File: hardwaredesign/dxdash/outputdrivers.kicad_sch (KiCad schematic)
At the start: 6 parts, among them J7 Power Low Side Outputs, Q2 NCV8402xST, Q3 NCV8402xST, U7 74HCT04

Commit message: controller board added features
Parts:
- renumbered J7 to J8
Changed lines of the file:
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@@
 		(dnp no)
 		(fields_autoplaced yes)
-		(property "Reference" "J7"
+		(property "Reference" "J8"
 			(at 149.86 100.3299 0)
 			(effects

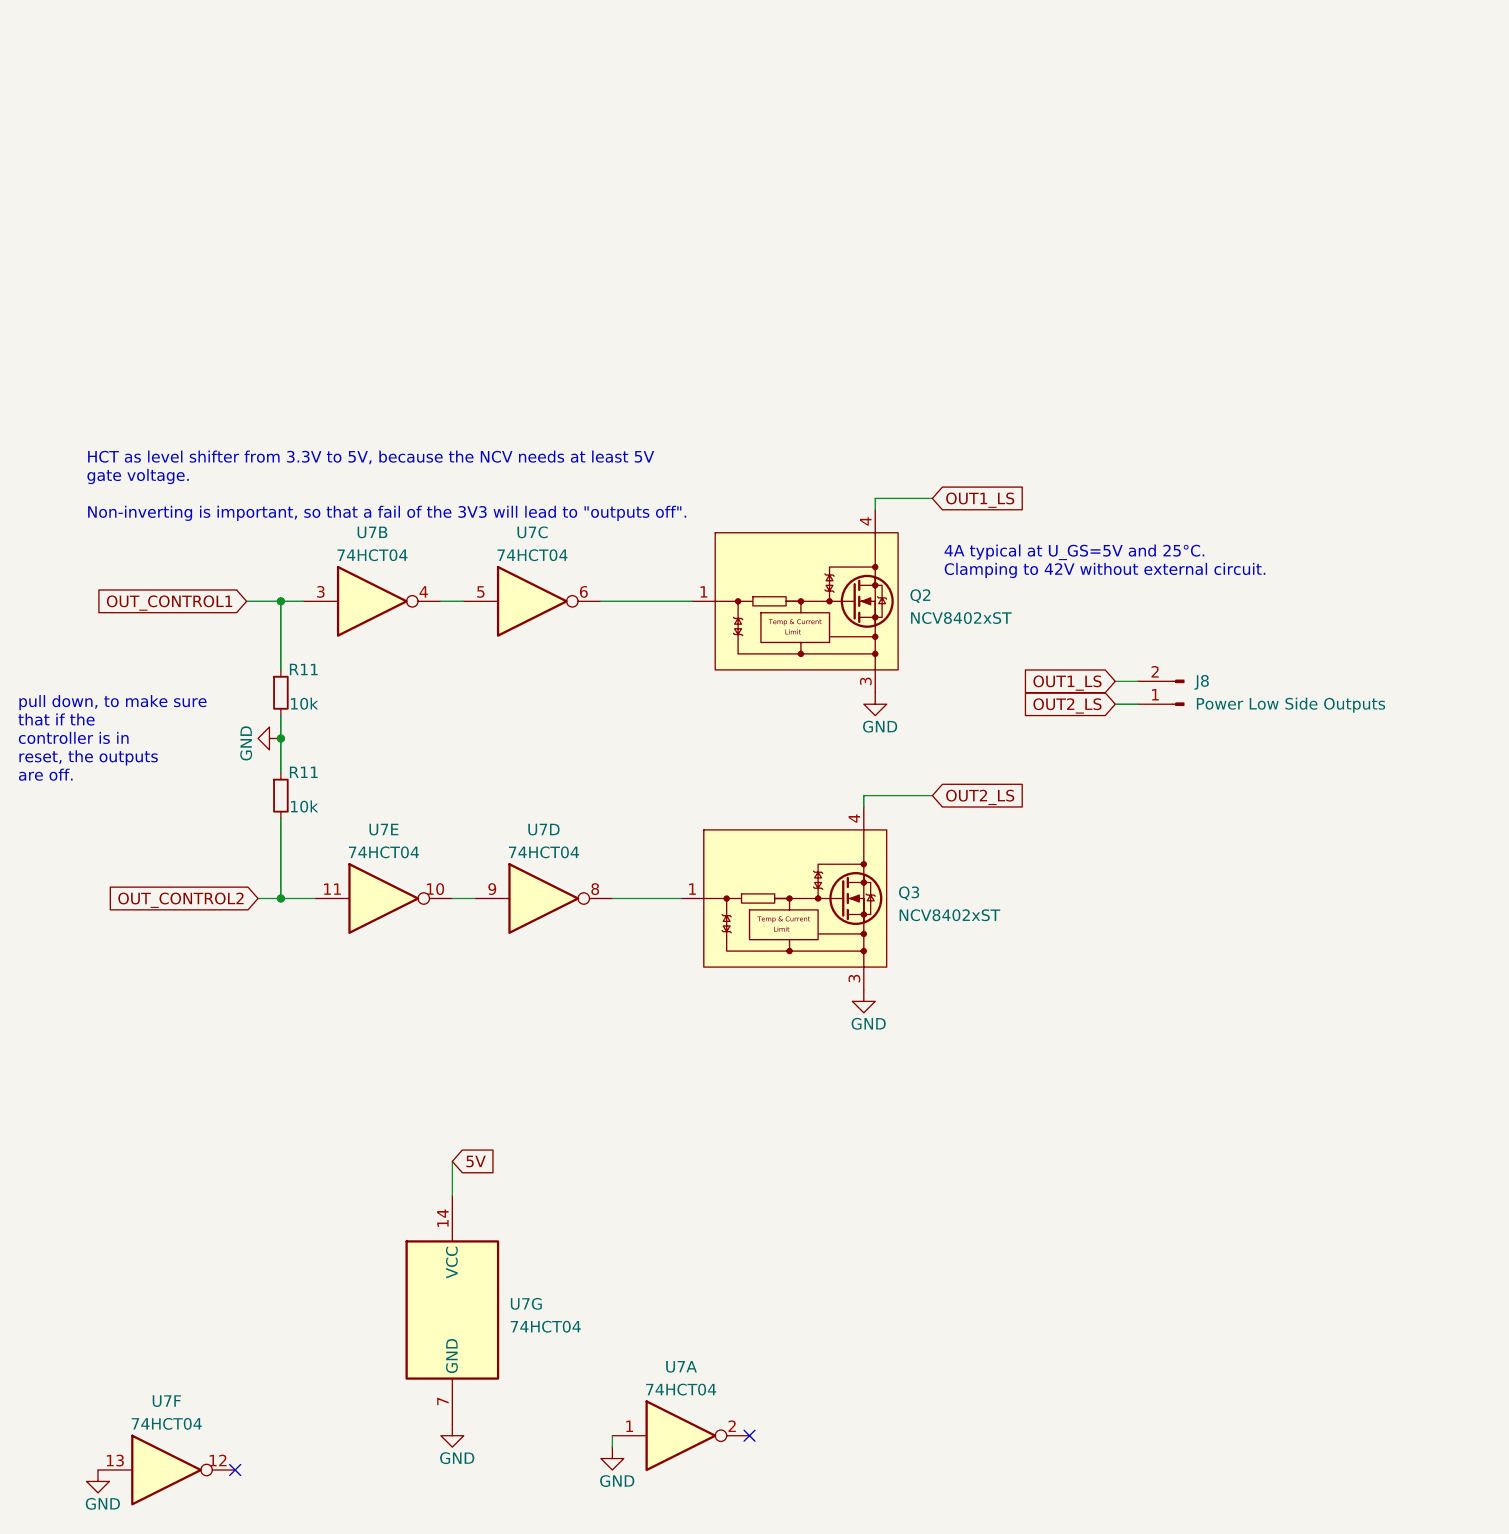
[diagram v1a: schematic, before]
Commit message: added polyfuses
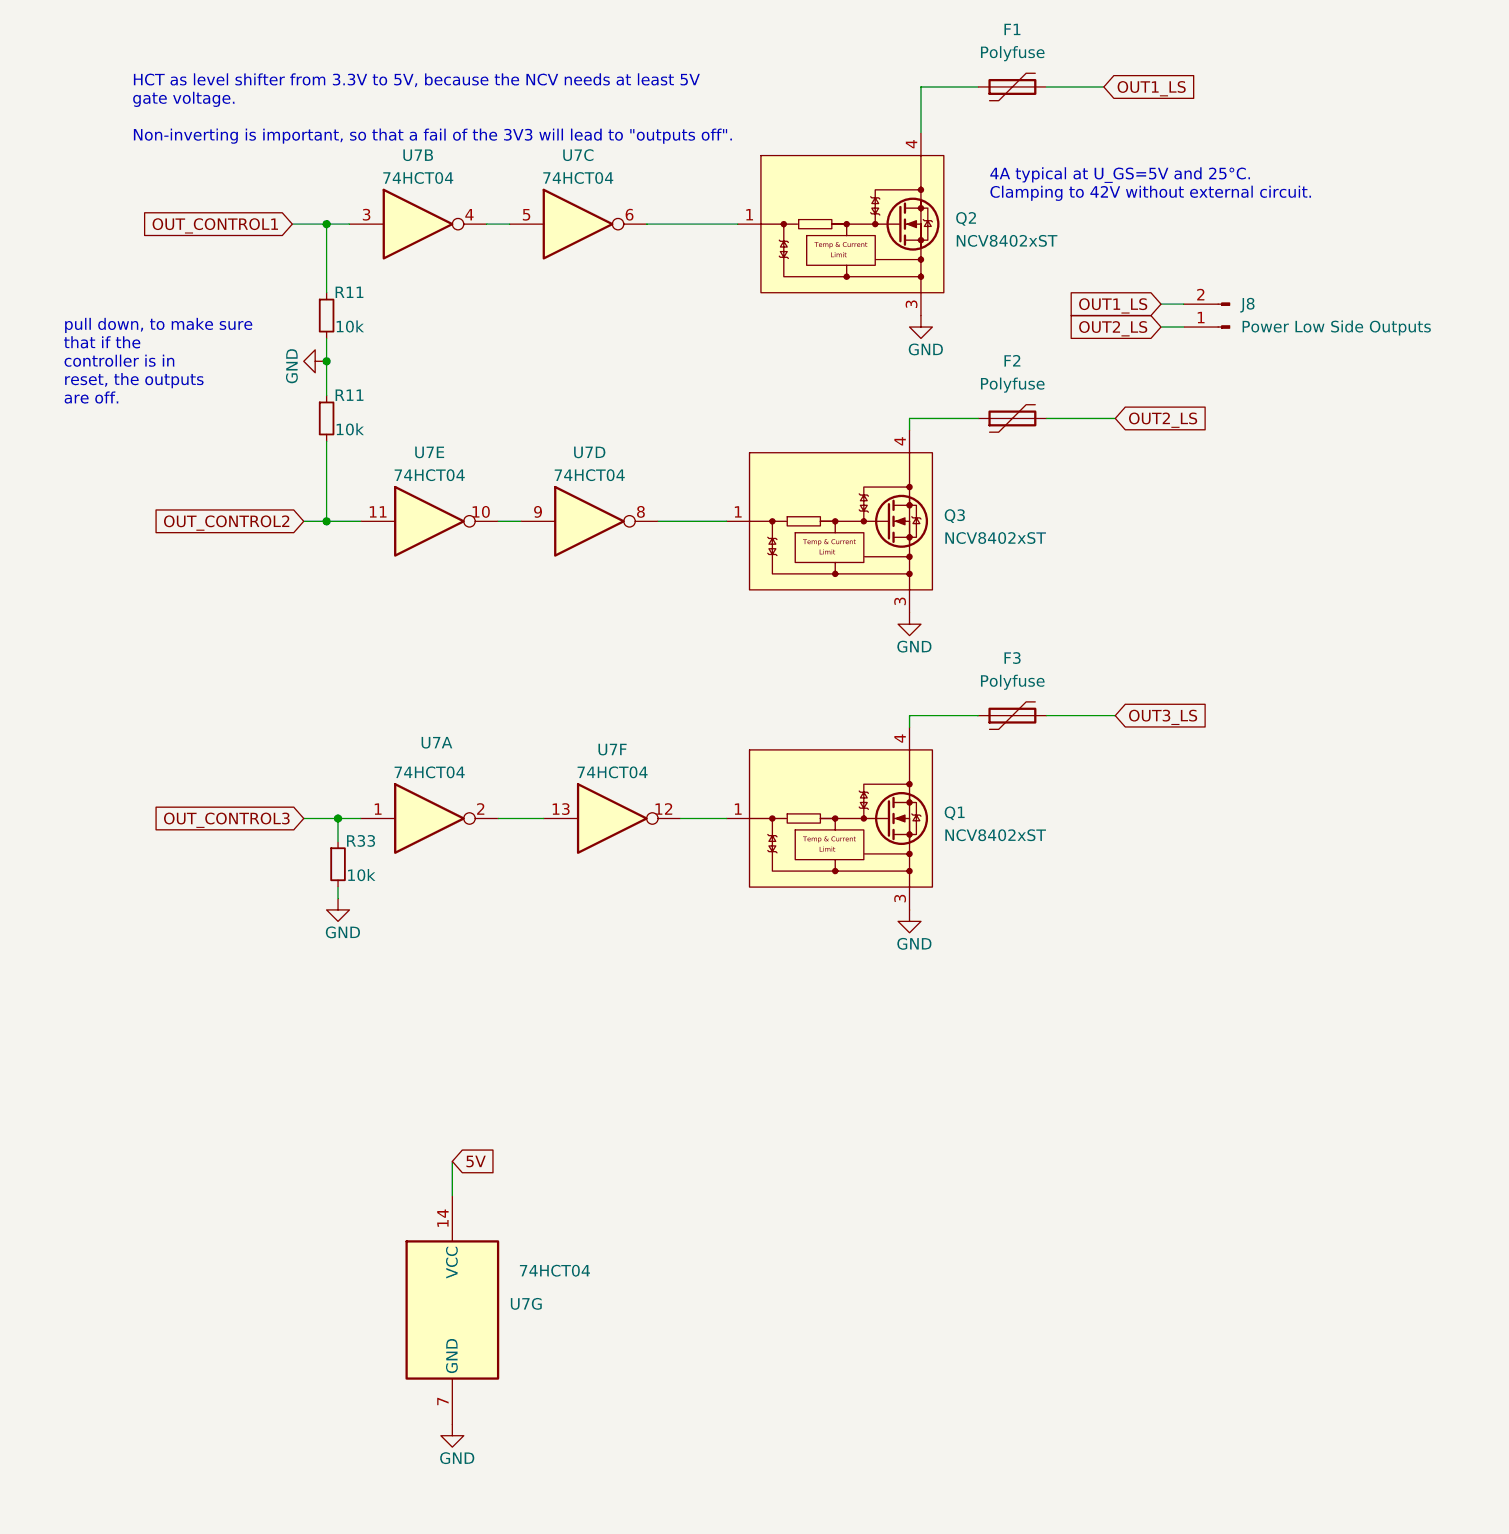
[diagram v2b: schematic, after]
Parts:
- added F1, F2, F3: Polyfuse, Fuse:Fuse_Bourns_MF-RG400, symbol Device:Polyfuse
- added Q1: NCV8402xST, Package_TO_SOT_SMD:SOT-223, symbol Driver_FET:NCV8402xST
- added R33: 10k, Resistor_SMD:R_1206_3216Metric_Pad1.30x1.75mm_HandSolder, symbol Device:R_Small
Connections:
- net GND: now also Q1.3 (S), R33.2; no longer U7.1, U7.13
- net OUT1_LS: now also F1.2; no longer Q2.2 (D), Q2.4 (D)
- net OUT2_LS: now also F2.2; no longer Q3.2 (D), Q3.4 (D)
- net at U7.2: now also U7.13
- net at U7.12: now also Q1.1 (G)
- new net: F3.1, Q1.2 (D), Q1.4 (D)
- new net: F1.1, Q2.2 (D), Q2.4 (D)
- new net: F2.1, Q3.2 (D), Q3.4 (D)
- new net OUT3_LS: F3.2
- new net OUT_CONTROL3: R33.1, U7.1
- no-connect marks 2 -> 0
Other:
- moved on the sheet: J8, Q2, Q3, R11, U7A, U7B, U7C, U7D, U7E, U7F

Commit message: more layout
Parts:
- removed J8: Power Low Side Outputs, Connector_PinHeader_2.54mm:PinHeader_1x02_P2.54mm_Vertical, symbol Connector:Conn_01x02_Pin
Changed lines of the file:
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@@
 	(wire
 		(pts
-			(xy 146.05 58.42) (xy 148.59 58.42)
+			(xy 72.39 115.57) (xy 77.47 115.57)
 		)
 		(stroke
@@
 	(wire
 		(pts
-			(xy 72.39 115.57) (xy 77.47 115.57)
+			(xy 50.8 115.57) (xy 54.61 115.57)
 		)
 		(stroke
@@
 	(wire
 		(pts
-			(xy 50.8 115.57) (xy 54.61 115.57)
+			(xy 54.61 123.19) (xy 54.61 124.46)
 		)
 		(stroke
@@
 	(wire
 		(pts
-			(xy 54.61 123.19) (xy 54.61 124.46)
+			(xy 133.35 71.12) (xy 140.97 71.12)
 		)
 		(stroke
@@
 	(wire
 		(pts
-			(xy 133.35 71.12) (xy 140.97 71.12)
-		)
-		(stroke
-			(width 0)
-			(type default)
-		)
-	)
-	(wire
-		(pts
 			(xy 50.8 82.55) (xy 53.34 82.55)
-		)
-		(stroke
-			(width 0)
-			(type default)
-		)
-	)
-	(wire
-		(pts
-			(xy 146.05 60.96) (xy 148.59 60.96)
 		)
 		(stroke
@@
 			)
 			(justify left bottom)
-		)
-	)
-	(global_label "OUT1_LS"
-		(shape input)
-		(at 146.05 58.42 180)
-		(fields_autoplaced yes)
-		(effects
-			(font
-				(size 1.27 1.27)
-			)
-			(justify right)
-		)
-		(property "Intersheetrefs" "${INTERSHEET_REFS}"
-			(at 135.0215 58.42 0)
-			(effects
-				(font
-					(size 1.27 1.27)
-				)
-				(justify right)
-				(hide yes)
-			)
 		)
 	)
@@
 		)
 	)
-	(global_label "OUT2_LS"
-		(shape input)
-		(at 146.05 60.96 180)
-		(fields_autoplaced yes)
-		(effects
-			(font
-				(size 1.27 1.27)
-			)
-			(justify right)
-		)
-		(property "Intersheetrefs" "${INTERSHEET_REFS}"
-			(at 135.0215 60.96 0)
-			(effects
-				(font
-					(size 1.27 1.27)
-				)
-				(justify right)
-				(hide yes)
-			)
-		)
-	)
 	(symbol
 		(lib_id "74xx:74HCT04")
@@
 				)
 			)
-		)
-	)
-	(symbol
-		(lib_id "Connector:Conn_01x02_Pin")
-		(at 153.67 60.96 180)
-		(unit 1)
-		(exclude_from_sim no)
-		(in_bom yes)
-		(on_board yes)
-		(dnp no)
-		(fields_autoplaced yes)
-		(property "Reference" "J8"
-			(at 154.94 58.4199 0)
-			(effects
-				(font
-					(size 1.27 1.27)
-				)
-				(justify right)
-			)
-		)
-		(property "Value" "Power Low Side Outputs"
-			(at 154.94 60.9599 0)
-			(effects
-				(font
-					(size 1.27 1.27)
-				)
-				(justify right)
-			)
-		)
-		(property "Footprint" "Connector_PinHeader_2.54mm:PinHeader_1x02_P2.54mm_Vertical"
-			(at 153.67 60.96 0)
-			(effects
-				(font
-					(size 1.27 1.27)
-				)
-				(hide yes)
-			)
-		)
-		(property "Datasheet" "~"
-			(at 153.67 60.96 0)
-			(effects
-				(font
-					(size 1.27 1.27)
-				)
-				(hide yes)
-			)
-		)
-		(property "Description" ""
-			(at 153.67 60.96 0)
-			(effects
-				(font
-					(size 1.27 1.27)
-				)
-				(hide yes)
-			)
-		)
-		(pin "1"
-		)
-		(pin "2"
-		)
-		(instances
-			(project "qca7000"
-				(path "/e63e39d7-6ac0-4ffd-8aa3-1841a4541b55/539ec63d-ac7e-42ea-858e-ff2bf33430ea"
-					(reference "J8")
-					(unit 1)
-				)
-				(path "/e63e39d7-6ac0-4ffd-8aa3-1841a4541b55/5666e7cf-6b6c-4583-8335-aa3be69ccd45"
-					(reference "J7")
-					(unit 1)
-				)
-			)
